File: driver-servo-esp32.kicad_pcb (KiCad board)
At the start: 2 copper layers, 55 x 55.9 mm, 64 parts, among them J1 USB_B, J3 Jack-DC, J5 USB_B, Q1 Q_NPN_BEC, Q2 Q_NPN_BEC, SW1 SW_Push, SW2 SW_Push, SW3 SW_DIP_x01, SW4 SW_DIP_x01, U1 ESP32-PICO-D4, U2 CP2102N-SHORT, U3 AMS1117-3.3, U4 CP2102N-SHORT, U5 74HC245

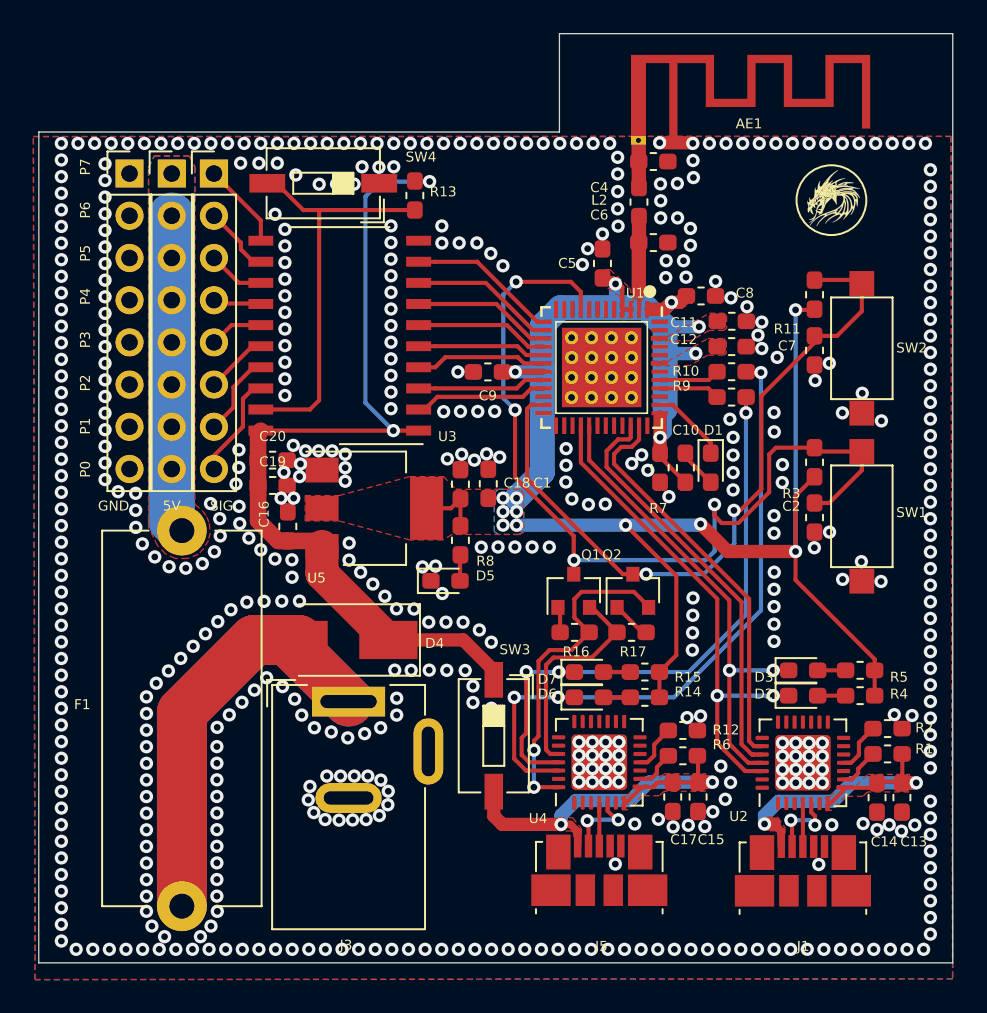
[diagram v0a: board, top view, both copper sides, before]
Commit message: remove auto flash
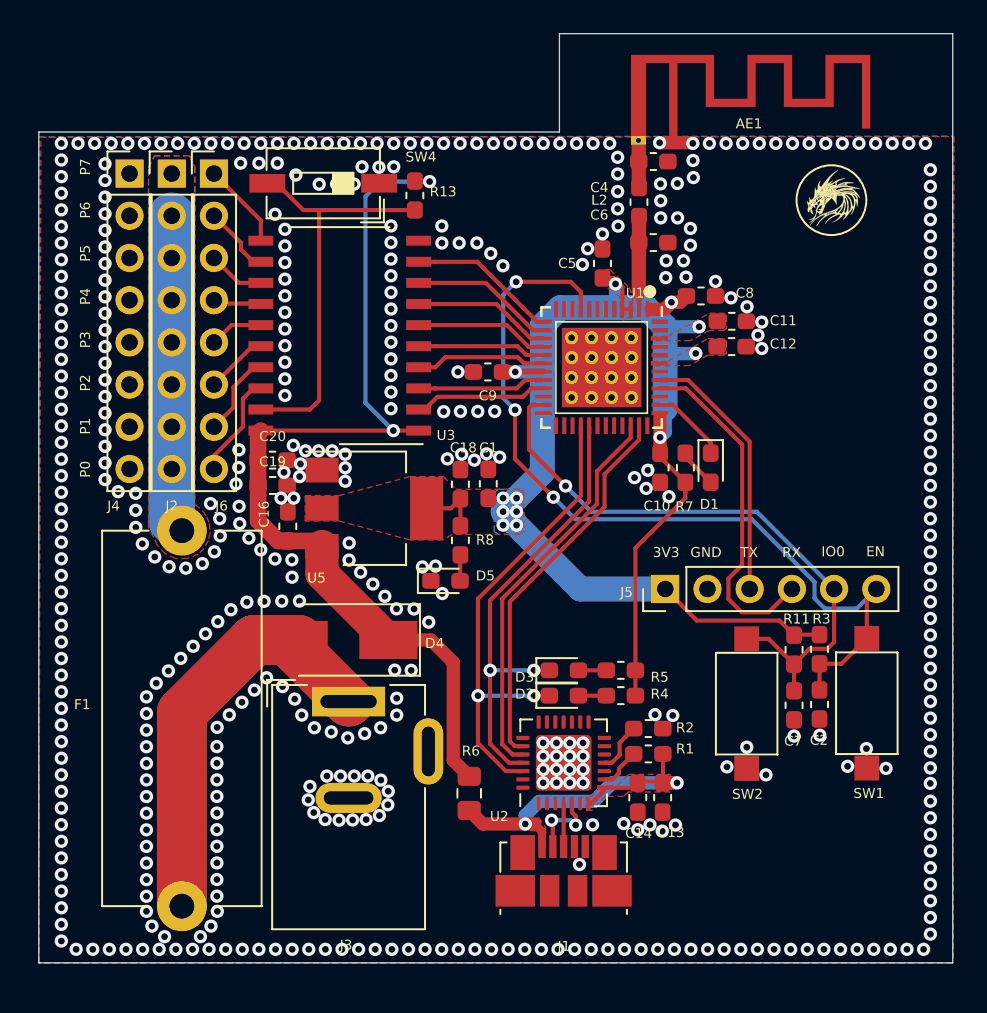
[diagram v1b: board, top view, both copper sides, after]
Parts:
- removed C15: 10uF, Capacitor_SMD:C_0603_1608Metric_Pad1.05x0.95mm_HandSolder
- removed C17: 100nF, Capacitor_SMD:C_0603_1608Metric_Pad1.05x0.95mm_HandSolder
- removed D6: TX, LED_SMD:LED_0603_1608Metric_Pad1.05x0.95mm_HandSolder
- removed D7: RX, LED_SMD:LED_0603_1608Metric_Pad1.05x0.95mm_HandSolder
- removed Q1, Q2: Q_NPN_BEC, Package_TO_SOT_SMD:SOT-23
- removed R10, R9: 470R, Resistor_SMD:R_0603_1608Metric_Pad1.05x0.95mm_HandSolder
- removed R12, R16, R17: 10K, Resistor_SMD:R_0603_1608Metric_Pad1.05x0.95mm_HandSolder
- removed R14, R15: 330R, Resistor_SMD:R_0603_1608Metric_Pad1.05x0.95mm_HandSolder
- removed SW3: SW_DIP_x01, Button_Switch_SMD:SW_DIP_SPSTx01_Slide_6.7x4.1mm_W6.73mm_P2.54mm_LowProfile_JPin
- removed U4: CP2102N-SHORT, Package_DFN_QFN:QFN-28-1EP_5x5mm_P0.5mm_EP3.35x3.35mm
- J5: value USB_B -> ESP_Flash; footprint Connector_USB:USB_Micro-B_Molex_47346-0001 -> Connector_PinHeader_2.54mm:PinHeader_1x06_P2.54mm_Vertical
- R6: value 4K7 -> 0R; footprint Resistor_SMD:R_0603_1608Metric_Pad1.05x0.95mm_HandSolder -> Resistor_SMD:R_0805_2012Metric_Pad1.15x1.40mm_HandSolder
- moved SW2 22.5 mm to (134.6, 131.9)
- moved R11 21.4 mm to (137.4, 128.7), turned to 270 degrees
- moved C7 21.4 mm to (137.4, 132.0)
- moved J5 17.4 mm to (129.7, 125.0), turned to 90 degrees
- moved C13 14.4 mm to (129.5, 137.6)
- moved J1 14.4 mm to (123.6, 142.0)
- moved R1 14.4 mm to (128.7, 134.9)
- moved R2 14.4 mm to (128.7, 133.4)
- moved R4 14.4 mm to (127.0, 131.4)
- moved R5 14.4 mm to (127.0, 129.9)
- moved U2 14.4 mm to (123.6, 135.5)
- moved D2 14.4 mm to (123.6, 131.4)
- moved D3 14.4 mm to (123.6, 129.9)
- moved C14 14.4 mm to (128.0, 137.6)
- moved R6 13.1 mm to (117.9, 137.3), turned to 270 degrees
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- renumbered 5V to J2, GND to J4, SIG to J6
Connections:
- J5 pad 1: VCCQ -> +3V3
- J5 pad 2: Net-(J5-Pad2) -> GND
- J5 pad 3: Net-(J5-Pad3) -> FLASH_U0TX
- J5 pad 4: GND -> FLASH_U0RX
- J5 pad 5: GND -> FLASH_IO0
- J5 pad 6: (no net) -> FLASH_EN
- R6 pad 1: VCCQ -> +5V
- R6 pad 2: Net-(R6-Pad2) -> VCCQ
- U1 pad 10: Net-(U1-Pad10) -> (no net)
- U1 pad 11: Net-(U1-Pad11) -> (no net)
- U1 pad 12: Net-(U1-Pad12) -> (no net)
- U1 pad 22: Net-(U1-Pad22) -> (no net)
- U1 pad 24: Net-(U1-Pad24) -> (no net)
- U1 pad 25: Net-(U1-Pad25) -> (no net)
- U1 pad 26: Net-(U1-Pad26) -> (no net)
- U1 pad 27: Net-(U1-Pad27) -> (no net)
- U1 pad 30: Net-(U1-Pad30) -> (no net)
- U1 pad 31: Net-(U1-Pad31) -> (no net)
- U1 pad 32: Net-(U1-Pad32) -> (no net)
- U1 pad 33: Net-(U1-Pad33) -> (no net)
- U1 pad 36: Net-(U1-Pad36) -> (no net)
- U1 pad 39: Net-(U1-Pad39) -> (no net)
- U1 pad 42: Net-(U1-Pad42) -> (no net)
- U1 pad 44: Net-(U1-Pad44) -> (no net)
- U1 pad 45: Net-(U1-Pad45) -> (no net)
- U1 pad 47: Net-(U1-Pad47) -> (no net)
- U1 pad 48: Net-(U1-Pad48) -> (no net)
- U1 pad 5: Net-(U1-Pad5) -> (no net)
- U1 pad 6: Net-(U1-Pad6) -> (no net)
- U1 pad 7: Net-(U1-Pad7) -> (no net)
- U1 pad 8: Net-(U1-Pad8) -> (no net)
- U2 pad 1: Net-(U2-Pad1) -> (no net)
- U2 pad 10: Net-(U2-Pad10) -> (no net)
- U2 pad 12: Net-(U2-Pad12) -> (no net)
- U2 pad 13: Net-(U2-Pad13) -> (no net)
- U2 pad 14: Net-(U2-Pad14) -> (no net)
- U2 pad 15: Net-(U2-Pad15) -> (no net)
- U2 pad 16: Net-(U2-Pad16) -> (no net)
- U2 pad 17: Net-(U2-Pad17) -> (no net)
- U2 pad 18: Net-(U2-Pad18) -> (no net)
- U2 pad 19: Net-(U2-Pad19) -> (no net)
- U2 pad 2: Net-(U2-Pad2) -> (no net)
- U2 pad 20: Net-(U2-Pad20) -> (no net)
- U2 pad 21: Net-(U2-Pad21) -> (no net)
- U2 pad 22: Net-(U2-Pad22) -> (no net)
- U2 pad 27: Net-(U2-Pad27) -> (no net)
- U2 pad 28: Net-(U2-Pad28) -> (no net)
- U2 pad 6: Net-(U2-Pad6) -> (no net)
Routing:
- net Net-(D6-Pad1): track 39.9 -> 0.00 mm, vias 3 -> 0
- net Net-(D7-Pad1): track 36.2 -> 0.00 mm, vias 3 -> 0
- net +3V3: track 112.5 -> 87.9 mm, vias 16 -> 12
- net VCCQ: track 46.0 -> 24.0 mm, vias 4 -> 2
- net FLASH_DTR: track 20.4 -> 0.00 mm, vias 2 -> 0
- net FLASH_U0RX: track 3.66 -> 20.7 mm
- net FLASH_RTS: track 13.3 -> 0.00 mm
- net FLASH_U0TX: track 3.65 -> 15.8 mm
- net FLASH_IO0: track 43.7 -> 36.5 mm, vias 2 -> 1
- net Net-(J5-Pad2): track 4.86 -> 0.00 mm, vias 2 -> 0
- net +5V: track 54.3 -> 58.4 mm
- net FLASH_EN: track 54.2 -> 51.3 mm, vias 4 -> 3
- net Net-(R12-Pad2): track 2.88 -> 0.00 mm
- net Net-(J5-Pad3): track 2.59 -> 0.00 mm
- net Net-(R6-Pad2): track 2.49 -> 0.00 mm
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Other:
- board text added: "3V3"
- board text added: "EN"
- board text added: "GND"
- board text added: "IO0"
- board text added: "RX"
- board text added: "TX"

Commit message: update demo
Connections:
- C20 pad 1: +5V -> (no net)
- C20 pad 2: GND -> (no net)
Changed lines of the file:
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@@
-(kicad_pcb (version 20171130) (host pcbnew 5.1.1-8be2ce7~80~ubuntu18.04.1)
+(kicad_pcb (version 20171130) (host pcbnew 5.1.4-e60b266~84~ubuntu18.04.1)
   (general
     (thickness 1.6)
@@
   (page A4)
   (layers
-    (0 F.Cu signal hide)
+    (0 F.Cu signal)
     (31 B.Cu signal)
     (32 B.Adhes user hide)
@@
       (net 1 GND))
     (pad 3 thru_hole oval (at 4.8 3 90) (size 4 1.8) (drill oval 3 0.8) (layers *.Cu *.Mask))
-    (model ${KISYS3DMOD}/Connector_BarrelJack.3dshapes/BarrelJack_Wuerth_6941xx301002.wrl
+    (model ${KISYS3DMOD}/Connector_BarrelJack.3dshapes/BarrelJack_CUI_PJ-063AH_Horizontal.wrl
       (at (xyz 0 0 0))
-      (scale (xyz 1 1 1))
+      (scale (xyz 0.9 1.1 1))
       (rotate (xyz 0 0 0))
     )
@@
     (fp_line (start -0.8 -0.4) (end 0.8 -0.4) (layer F.Fab) (width 0.1))
     (fp_line (start -0.8 0.4) (end -0.8 -0.4) (layer F.Fab) (width 0.1))
-    (pad 2 smd roundrect (at 0.875 0) (size 1.05 0.95) (layers F.Cu F.Paste F.Mask) (roundrect_rratio 0.25)
-      (net 1 GND))
-    (pad 1 smd roundrect (at -0.875 0) (size 1.05 0.95) (layers F.Cu F.Paste F.Mask) (roundrect_rratio 0.25)
-      (net 6 +5V))
+    (pad 2 smd roundrect (at 0.875 0) (size 1.05 0.95) (layers F.Cu F.Paste F.Mask) (roundrect_rratio 0.25))
+    (pad 1 smd roundrect (at -0.875 0) (size 1.05 0.95) (layers F.Cu F.Paste F.Mask) (roundrect_rratio 0.25))
     (model ${KISYS3DMOD}/Capacitor_SMD.3dshapes/C_0603_1608Metric.wrl
       (at (xyz 0 0 0))
@@
   (gr_line (start 92 97.5) (end 123.3297 97.5) (layer Edge.Cuts) (width 0.05))
   (gr_line (start 91.9988 147.5) (end 92 97.5) (layer Edge.Cuts) (width 0.05))
-  (gr_line (start 147 147.5) (end 92 147.5) (layer Edge.Cuts) (width 0.05))
+  (gr_line (start 147 147.5) (end 91.9988 147.5) (layer Edge.Cuts) (width 0.05))
   (gr_line (start 147 91.5797) (end 147 147.5) (layer Edge.Cuts) (width 0.05))
   (via (at 127.205 139.1158) (size 0.8) (drill 0.4) (layers F.Cu B.Cu) (net 1))
@@
     (connect_pads yes (clearance 0.2))
     (min_thickness 0.254)
-    (fill yes (arc_segments 32) (thermal_gap 0.508) (thermal_bridge_width 0.508))
+    (fill (arc_segments 32) (thermal_gap 0.508) (thermal_bridge_width 0.508))
     (polygon
       (pts
@@
     (connect_pads yes (clearance 0.2))
     (min_thickness 0.254)
-    (fill yes (arc_segments 32) (thermal_gap 0.508) (thermal_bridge_width 0.508))
+    (fill (arc_segments 32) (thermal_gap 0.508) (thermal_bridge_width 0.508))
     (polygon
       (pts
@@
     (connect_pads yes (clearance 0.2))
     (min_thickness 0.254)
-    (fill yes (arc_segments 32) (thermal_gap 0.508) (thermal_bridge_width 0.508))
+    (fill (arc_segments 32) (thermal_gap 0.508) (thermal_bridge_width 0.508))
     (polygon
       (pts
@@
     (connect_pads yes (clearance 0.2))
     (min_thickness 0.254)
-    (fill yes (arc_segments 32) (thermal_gap 0.508) (thermal_bridge_width 0.508))
+    (fill (arc_segments 32) (thermal_gap 0.508) (thermal_bridge_width 0.508))
     (polygon
       (pts
@@
     (connect_pads yes (clearance 0.2))
     (min_thickness 0.254)
-    (fill yes (arc_segments 32) (thermal_gap 0.508) (thermal_bridge_width 0.508))
+    (fill (arc_segments 32) (thermal_gap 0.508) (thermal_bridge_width 0.508))
     (polygon
       (pts
@@
     (connect_pads yes (clearance 0.2))
     (min_thickness 0.254)
-    (fill yes (arc_segments 32) (thermal_gap 0.508) (thermal_bridge_width 0.508))
+    (fill (arc_segments 32) (thermal_gap 0.508) (thermal_bridge_width 0.508))
     (polygon
       (pts
@@
     (connect_pads yes (clearance 0.2))
     (min_thickness 0.254)
-    (fill yes (arc_segments 32) (thermal_gap 0.508) (thermal_bridge_width 0.508))
+    (fill (arc_segments 32) (thermal_gap 0.508) (thermal_bridge_width 0.508))
     (polygon
       (pts
@@
     (connect_pads yes (clearance 0.2))
     (min_thickness 0.254)
-    (fill yes (arc_segments 32) (thermal_gap 0.508) (thermal_bridge_width 0.508))
+    (fill (arc_segments 32) (thermal_gap 0.508) (thermal_bridge_width 0.508))
     (polygon
       (pts
@@
     (connect_pads yes (clearance 0.2))
     (min_thickness 0.254)
-    (fill yes (arc_segments 32) (thermal_gap 0.508) (thermal_bridge_width 0.508))
+    (fill (arc_segments 32) (thermal_gap 0.508) (thermal_bridge_width 0.508))
     (polygon
       (pts
@@
     (connect_pads yes (clearance 0.2))
     (min_thickness 0.254)
-    (fill yes (arc_segments 32) (thermal_gap 0.508) (thermal_bridge_width 0.508))
+    (fill (arc_segments 32) (thermal_gap 0.508) (thermal_bridge_width 0.508))
     (polygon
       (pts
@@
     (connect_pads yes (clearance 0.2))
     (min_thickness 0.2)
-    (fill yes (arc_segments 32) (thermal_gap 0.508) (thermal_bridge_width 0.508))
+    (fill (arc_segments 32) (thermal_gap 0.508) (thermal_bridge_width 0.508))
     (polygon
       (pts
@@
     (connect_pads yes (clearance 0.2))
     (min_thickness 0.2)
-    (fill yes (arc_segments 32) (thermal_gap 0.508) (thermal_bridge_width 0.508))
+    (fill (arc_segments 32) (thermal_gap 0.508) (thermal_bridge_width 0.508))
     (polygon
       (pts
